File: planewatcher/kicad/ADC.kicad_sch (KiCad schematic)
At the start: 15 parts, among them U11 AD9203ARUZ

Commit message: Add persistent PCBWay BOM fields to KiCad schematic
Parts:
- C49, C52, C55, C58: MPN (none) -> GRM188R61C106MA73D; Manufacturer (none) -> Murata; Package (none) -> 0603
- C50, C51, C53, C54, C56, C57: MPN (none) -> GRM155R71H104KE14D; Manufacturer (none) -> Murata; Package (none) -> 0402
- RN2, RN3, RN4: MPN (none) -> CAT16-2201F4LF; Manufacturer (none) -> Bourns; Package (none) -> 1206 array (CAT16-4)
- U11: MPN (none) -> AD9203ARUZ; Manufacturer (none) -> Analog Devices; Package (none) -> TSSOP-28

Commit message: move power supply and add GPS module
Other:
- title: Plane Watcher: ADC Section -> Plane Watcher
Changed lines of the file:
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@@
 	(paper "A4")
 	(title_block
-		(title "Plane Watcher: ADC Section")
-		(date "2026-05-16")
-		(rev "prototype 1.1")
+		(title "Plane Watcher")
+		(date "2026-05-18")
+		(rev "prototype 1.2")
 		(company "plane.watch")
 	)

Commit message: fix incorrect part number
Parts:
- RN2, RN3, RN4: MPN CAT16-2201F4LF -> CAT16-22R0F4LF; Suggested Part Bourns CAT16-2201F4LF -> Bourns CAT16-22R0F4LF
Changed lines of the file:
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@@
 			)
 		)
-		(property "MPN" "CAT16-2201F4LF"
+		(property "MPN" "CAT16-22R0F4LF"
 			(at 45.72 85.09 0)
 			(hide yes)
@@
 			)
 		)
-		(property "Suggested Part" "Bourns CAT16-2201F4LF"
+		(property "Suggested Part" "Bourns CAT16-22R0F4LF"
 			(at 45.72 85.09 0)
 			(hide yes)
@@
 			)
 		)
-		(property "MPN" "CAT16-2201F4LF"
+		(property "MPN" "CAT16-22R0F4LF"
 			(at 58.42 74.93 0)
 			(hide yes)
@@
 			)
 		)
-		(property "Suggested Part" "Bourns CAT16-2201F4LF"
+		(property "Suggested Part" "Bourns CAT16-22R0F4LF"
 			(at 58.42 74.93 0)
 			(hide yes)
@@
 			)
 		)
-		(property "MPN" "CAT16-2201F4LF"
+		(property "MPN" "CAT16-22R0F4LF"
 			(at 45.72 93.98 0)
 			(hide yes)
@@
 			)
 		)
-		(property "Suggested Part" "Bourns CAT16-2201F4LF"
+		(property "Suggested Part" "Bourns CAT16-22R0F4LF"
 			(at 45.72 93.98 0)
 			(hide yes)

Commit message: review & consolidate all capacitors
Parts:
- C49, C52, C55, C58: MPN GRM188R61C106MA73D -> GRM188Z71A106MA73J; Manufacturer Murata -> Murata Electronics; Package 0603 -> 0603 (1608 Metric); Suggested Part Murata GRM188R61C106MA73D -> (none)
- C50, C51, C53, C54, C56, C57: value 0.1µF -> 100nF; MPN GRM155R71H104KE14D -> GCM155R71A104KA55D; Manufacturer Murata -> Murata Electronics; Package 0402 -> 0402 (1005 Metric); Suggested Part Murata GRM155R71H104KE14D -> (none)
- RN2, RN3, RN4: Suggested Part Bourns CAT16-22R0F4LF -> (none)
- TP21: Suggested Part No fitted part (PCB pad only) -> (none)
- U11: Suggested Part Analog Devices AD9203ARUZ -> (none)

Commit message: review & consolidate all resistors
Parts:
- RN2, RN3, RN4: Manufacturer Bourns -> Bourns Inc.
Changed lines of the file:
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@@
 			)
 		)
-		(property "Datasheet" "https://au.mouser.com/datasheet/3/40/1/CATCAY.pdf"
+		(property "Datasheet" "https://www.bourns.com/docs/Product-Datasheets/CATCAY.pdf"
 			(at 45.72 85.09 0)
 			(hide yes)
@@
 			)
 		)
-		(property "Manufacturer" "Bourns"
+		(property "Manufacturer" "Bourns Inc."
 			(at 45.72 85.09 0)
 			(hide yes)
@@
 			)
 		)
-		(property "Datasheet" "https://au.mouser.com/datasheet/3/40/1/CATCAY.pdf"
+		(property "Datasheet" "https://www.bourns.com/docs/Product-Datasheets/CATCAY.pdf"
 			(at 58.42 74.93 0)
 			(hide yes)
@@
 			)
 		)
-		(property "Manufacturer" "Bourns"
+		(property "Manufacturer" "Bourns Inc."
 			(at 58.42 74.93 0)
 			(hide yes)
@@
 			)
 		)
-		(property "Datasheet" "https://au.mouser.com/datasheet/3/40/1/CATCAY.pdf"
+		(property "Datasheet" "https://www.bourns.com/docs/Product-Datasheets/CATCAY.pdf"
 			(at 45.72 93.98 0)
 			(hide yes)
@@
 			)
 		)
-		(property "Manufacturer" "Bourns"
+		(property "Manufacturer" "Bourns Inc."
 			(at 45.72 93.98 0)
 			(hide yes)

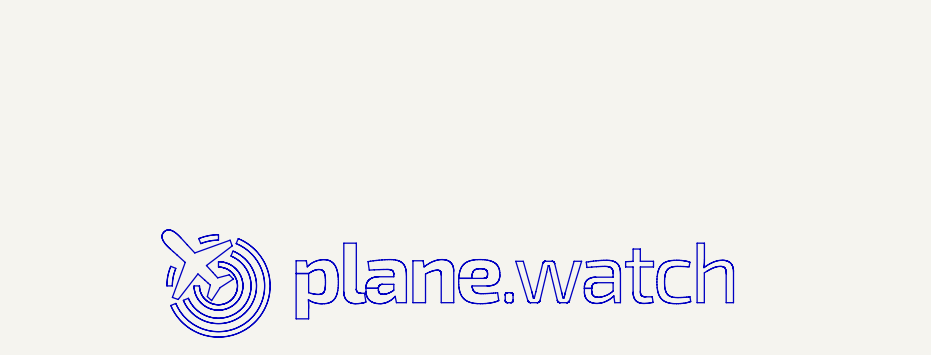
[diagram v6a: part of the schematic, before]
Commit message: add license & copyright info to schematic and pcb. fix layer window.
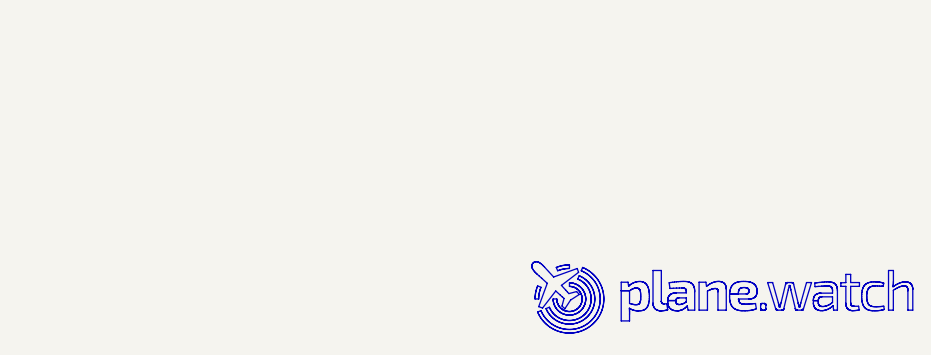
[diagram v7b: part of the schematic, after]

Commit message: added lcsc_ids to all parts
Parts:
- C49, C52, C55, C58: MPN GRM188Z71A106MA73J -> GRM188Z71A106MA73D; lcsc_id (none) -> C237435
- C50, C51, C53, C54, C56, C57: lcsc_id (none) -> C161163
- RN2, RN3, RN4: lcsc_id (none) -> C1731387
- U11: lcsc_id (none) -> C653239
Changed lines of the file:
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@@
 			)
 		)
-		(property "MPN" "GRM188Z71A106MA73J"
+		(property "MPN" "GRM188Z71A106MA73D"
 			(at 135.89 101.6 0)
 			(hide yes)
@@
 		)
 		(property "Purpose" "Local bulk decoupling for AD9203 analog, digital, and reference supply rails."
+			(at 135.89 101.6 0)
+			(hide yes)
+			(show_name no)
+			(do_not_autoplace no)
+			(effects
+				(font
+					(size 1.27 1.27)
+				)
+			)
+		)
+		(property "lcsc_id" "C237435"
 			(at 135.89 101.6 0)
 			(hide yes)
@@
 			)
 		)
+		(property "lcsc_id" "C161163"
+			(at 121.92 101.6 0)
+			(hide yes)
+			(show_name no)
+			(do_not_autoplace no)
+			(effects
+				(font
+					(size 1.27 1.27)
+				)
+			)
+		)
 		(pin "1"
 		)
@@
 		)
 		(property "Purpose" "Series damping/termination for AD9203 digital output lines into the FPGA header."
+			(at 45.72 85.09 0)
+			(hide yes)
+			(show_name no)
+			(do_not_autoplace no)
+			(effects
+				(font
+					(size 1.27 1.27)
+				)
+			)
+		)
+		(property "lcsc_id" "C1731387"
 			(at 45.72 85.09 0)
 			(hide yes)
@@
 			)
 		)
-		(property "MPN" "GRM188Z71A106MA73J"
+		(property "MPN" "GRM188Z71A106MA73D"
 			(at 135.89 77.47 0)
 			(hide yes)
@@
 		)
 		(property "Purpose" "Local bulk decoupling for AD9203 analog, digital, and reference supply rails."
+			(at 135.89 77.47 0)
+			(hide yes)
+			(show_name no)
+			(do_not_autoplace no)
+			(effects
+				(font
+					(size 1.27 1.27)
+				)
+			)
+		)
+		(property "lcsc_id" "C237435"
 			(at 135.89 77.47 0)
 			(hide yes)
@@
 			)
 		)
+		(property "lcsc_id" "C161163"
+			(at 121.92 77.47 0)
+			(hide yes)
+			(show_name no)
+			(do_not_autoplace no)
+			(effects
+				(font
+					(size 1.27 1.27)
+				)
+			)
+		)
 		(pin "1"
 		)
@@
 			)
 		)
+		(property "lcsc_id" "C161163"
+			(at 59.69 58.42 0)
+			(hide yes)
+			(show_name no)
+			(do_not_autoplace no)
+			(effects
+				(font
+					(size 1.27 1.27)
+				)
+			)
+		)
 		(pin "1"
 		)
@@
 			)
 		)
+		(property "lcsc_id" "C161163"
+			(at 107.95 58.42 0)
+			(hide yes)
+			(show_name no)
+			(do_not_autoplace no)
+			(effects
+				(font
+					(size 1.27 1.27)
+				)
+			)
+		)
 		(pin "1"
 		)
@@
 			)
 		)
-		(property "MPN" "GRM188Z71A106MA73J"
+		(property "MPN" "GRM188Z71A106MA73D"
 			(at 121.92 58.42 0)
 			(hide yes)
@@
 		)
 		(property "Purpose" "Local bulk decoupling for AD9203 analog, digital, and reference supply rails."
+			(at 121.92 58.42 0)
+			(hide yes)
+			(show_name no)
+			(do_not_autoplace no)
+			(effects
+				(font
+					(size 1.27 1.27)
+				)
+			)
+		)
+		(property "lcsc_id" "C237435"
 			(at 121.92 58.42 0)
 			(hide yes)
@@
 			)
 		)
+		(property "lcsc_id" "C653239"
+			(at 83.82 49.53 0)
+			(hide yes)
+			(show_name no)
+			(do_not_autoplace no)
+			(effects
+				(font
+					(size 1.27 1.27)
+				)
+			)
+		)
 		(pin "19"
 		)
@@
 			)
 		)
-		(property "MPN" "GRM188Z71A106MA73J"
+		(property "MPN" "GRM188Z71A106MA73D"
 			(at 45.72 58.42 0)
 			(hide yes)
@@
 		)
 		(property "Purpose" "Local bulk decoupling for AD9203 analog, digital, and reference supply rails."
+			(at 45.72 58.42 0)
+			(hide yes)
+			(show_name no)
+			(do_not_autoplace no)
+			(effects
+				(font
+					(size 1.27 1.27)
+				)
+			)
+		)
+		(property "lcsc_id" "C237435"
 			(at 45.72 58.42 0)
 			(hide yes)
@@
 			)
 		)
+		(property "lcsc_id" "C161163"
+			(at 152.4 81.28 0)
+			(hide yes)
+			(show_name no)
+			(do_not_autoplace no)
+			(effects
+				(font
+					(size 1.27 1.27)
+				)
+			)
+		)
 		(pin "1"
 		)
@@
 			)
 		)
+		(property "lcsc_id" "C1731387"
+			(at 58.42 74.93 0)
+			(hide yes)
+			(show_name no)
+			(do_not_autoplace no)
+			(effects
+				(font
+					(size 1.27 1.27)
+				)
+			)
+		)
 		(pin "8"
 		)
@@
 			)
 		)
+		(property "lcsc_id" "C1731387"
+			(at 45.72 93.98 0)
+			(hide yes)
+			(show_name no)
+			(do_not_autoplace no)
+			(effects
+				(font
+					(size 1.27 1.27)
+				)
+			)
+		)
 		(pin "8"
 		)
@@
 			(at 152.4 73.66 0)
 			(hide yes)
+			(show_name no)
+			(do_not_autoplace no)
+			(effects
+				(font
+					(size 1.27 1.27)
+				)
+			)
+		)
+		(property "lcsc_id" "C161163"
+			(at 152.4 73.66 0)
+			(hide yes)
